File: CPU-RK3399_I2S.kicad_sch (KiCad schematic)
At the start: 1 part, among them U1 RK3399

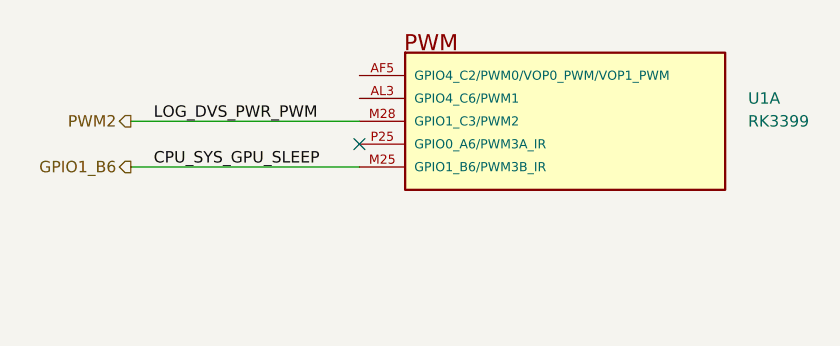
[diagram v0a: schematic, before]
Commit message: update schematic
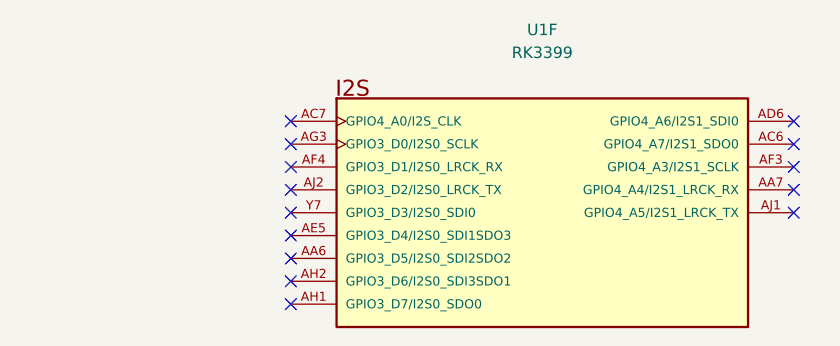
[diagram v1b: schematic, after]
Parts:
- removed U1: RK3399, footprints:BGA828C65P31X31_2100X2100X161, symbol component_library:System On Chip (SoC)/RK3399
- added U1: RK3399, footprints:BGA828C65P31X31_2100X2100X161, symbol component_library:System On Chip (SoC)/RK3399
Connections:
- no-connect marks 1 -> 14
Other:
- title: (none) -> CPU-RK3399 I2S Controller
